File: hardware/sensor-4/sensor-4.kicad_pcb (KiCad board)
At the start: 2 copper layers, 11 x 32 mm, 13 parts, among them J101 2x05_Horizontal, U101 A31010SEHALT-10

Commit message: Replace Order_Number
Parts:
- C101: footprint Capacitor_SMD:C_0603_1608Metric -> V2_Capacitor_SMD:C_0603
- FID101, FID102: value Fiducial -> Fiducial_Paste
- H101, H102, H103: value MountingHole_2.5mm -> 2.5mm
- INFO101: value ORDER-NUMBER -> ~; footprint V2_Production:Order_Number -> V2_Production:Revision
- moved INFO101 2.30 mm to (163.8, 169.8)
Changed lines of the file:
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@@
 	(paper "A4")
 	(title_block
-		(date "2023-07-17")
-		(rev "1")
+		(date "2026-02-13")
+		(rev "2026-02-13")
 	)
 	(layers
@@
 			)
 		)
-		(property "Value" "Fiducial"
+		(property "Value" "Fiducial_Paste"
 			(at 0 1.5 0)
 			(layer "F.Fab")
@@
 			)
 		)
-		(property "Description" "Fiducial Marker"
+		(property "Description" ""
 			(at 0 0 0)
 			(unlocked yes)
@@
 		(at 159.75 171 180)
 		(property "Reference" "J101"
-			(at -1.27 -7.62 0)
+			(at -1.27 -7.62 180)
 			(layer "F.SilkS")
 			(hide yes)
@@
 					(thickness 0.065024)
 				)
-				(justify right top)
+				(justify left bottom)
 			)
 		)
 		(property "Value" "2x05_Horizontal"
-			(at -1.778 3.81 0)
+			(at -1.778 3.81 180)
 			(layer "F.Fab")
 			(hide yes)
@@
 					(thickness 0.065024)
 				)
-				(justify right top)
-			)
-		)
-		(property "Datasheet" "~"
+				(justify left bottom)
+			)
+		)
+		(property "Datasheet" ""
 			(at 0 0 180)
 			(unlocked yes)
@@
 			(end -3.175 -1.2)
 			(stroke
-				(width 0.127)
-				(type solid)
-			)
-			(layer "F.SilkS")
-		)
-		(fp_line
-			(start 3.175 -3.7)
-			(end 3.175 -1.2)
-			(stroke
-				(width 0.127)
+				(width 0.1)
 				(type solid)
 			)
@@
 			(end 3.175 -3.7)
 			(stroke
-				(width 0.127)
+				(width 0.1)
 				(type solid)
 			)
@@
 			(end 2.54 -3.7)
 			(stroke
-				(width 0.127)
+				(width 0.1)
 				(type solid)
 			)
@@
 			(end -1.27 -3.7)
 			(stroke
-				(width 0.127)
-				(type solid)
-			)
-			(layer "F.SilkS")
-		)
-		(fp_line
-			(start -3.175 -1.2)
-			(end -3.175 -3.7)
-			(stroke
-				(width 0.127)
+				(width 0.1)
 				(type solid)
 			)
@@
 			(end -2.54 -3.7)
 			(stroke
-				(width 0.127)
-				(type solid)
-			)
+				(width 0.1)
+				(type solid)
+			)
+			(layer "F.SilkS")
+		)
+		(fp_poly
+			(pts
+				(xy 4.01 0.155) (xy 3.77 -0.175) (xy 4.25 -0.175) (xy 4.01 0.155)
+			)
+			(stroke
+				(width 0.12)
+				(type solid)
+			)
+			(fill yes)
 			(layer "F.SilkS")
 		)
@@
 			)
 			(layer "F.Fab")
+		)
+		(fp_text user "${REFERENCE}"
+			(at 0 -2.4 180)
+			(layer "F.Fab")
+			(effects
+				(font
+					(size 0.5 0.5)
+					(thickness 0.1)
+					(bold yes)
+				)
+			)
 		)
 		(pad "" smd roundrect
@@
 		)
 		(embedded_fonts no)
-		(model "../../3dmodels/V2_Connector_PinHeader_1.27mm.3dshapes/PinHeader_2x05_P1.27mm.stp"
+		(model "../../3dmodels/V2_Connector_PinHeader_1.27mm.3dshapes/PinHeader_2x05_P1.27mm_Horizontal.step"
 			(offset
 				(xyz 2.52 1.18 1.65)
@@
 			)
 		)
-		(property "Value" "MountingHole_2.5mm"
+		(property "Value" "2.5mm"
 			(at 0 2.23 0)
 			(unlocked yes)
@@
 			)
 		)
-		(property "Description" "Mounting Hole without connection"
+		(property "Description" ""
 			(at 0 0 0)
 			(unlocked yes)
@@
 			)
 		)
-		(property "Value" "Fiducial"
+		(property "Value" "Fiducial_Paste"
 			(at 0 1.5 0)
 			(layer "F.Fab")
@@
 			)
 		)
-		(property "Description" "Fiducial Marker"
+		(property "Description" ""
 			(at 0 0 0)
 			(unlocked yes)
@@
 			)
 		)
-		(property "Value" "MountingHole_2.5mm"
+		(property "Value" "2.5mm"
 			(at 0 2.23 0)
 			(unlocked yes)
@@
 			)
 		)
-		(property "Description" "Mounting Hole without connection"
+		(property "Description" ""
 			(at 0 0 0)
 			(unlocked yes)
@@
 		(embedded_fonts no)
 	)
-	(footprint "Capacitor_SMD:C_0603_1608Metric"
+	(footprint "V2_Capacitor_SMD:C_0603"
 		(layer "F.Cu")
 		(at 159.75 162.75)
@@
 			)
 		)
-		(property "Datasheet" "~"
+		(property "Datasheet" ""
 			(at 0 0 0)
 			(layer "F.Fab")
@@
 			)
 		)
-		(property "Description" "Unpolarized capacitor, small symbol"
+		(property "Description" ""
 			(at 0 0 0)
 			(layer "F.Fab")
@@
 		)
 		(fp_rect
-			(start -1.48 -0.73)
-			(end 1.48 0.73)
+			(start -1.23 -0.73)
+			(end 1.23 0.73)
 			(stroke
 				(width 0.05)
@@
 			(effects
 				(font
-					(size 0.4 0.4)
-					(thickness 0.06)
-				)
-			)
+					(size 0.3 0.3)
+					(thickness 0.05)
+				)
+			)
+		)
+		(pad "" smd roundrect
+			(at -0.7 0)
+			(size 0.7 0.8)
+			(layers "F.Paste")
+			(roundrect_rratio 0.1428571429)
+			(chamfer_ratio 0.3)
+			(chamfer top_right bottom_right)
+		)
+		(pad "" smd roundrect
+			(at 0.7 0)
+			(size 0.7 0.8)
+			(layers "F.Paste")
+			(roundrect_rratio 0.1428571429)
+			(chamfer_ratio 0.3)
+			(chamfer top_left bottom_left)
 		)
 		(pad "1" smd roundrect
-			(at -0.775 0)
-			(size 0.9 0.95)
-			(layers "F.Cu" "F.Mask" "F.Paste")
-			(roundrect_rratio 0.25)
+			(at -0.7 0)
+			(size 0.7 0.8)
+			(layers "F.Cu" "F.Mask")
+			(roundrect_rratio 0.1428571429)
 			(net 1 "+3V3")
 			(pintype "passive")
 		)
 		(pad "2" smd roundrect
-			(at 0.775 0)
-			(size 0.9 0.95)
-			(layers "F.Cu" "F.Mask" "F.Paste")
-			(roundrect_rratio 0.25)
+			(at 0.7 0)
+			(size 0.7 0.8)
+			(layers "F.Cu" "F.Mask")
+			(roundrect_rratio 0.1428571429)
 			(net 4 "GND")
 			(pintype "passive")
 		)
 		(embedded_fonts no)
-		(model "${KICAD9_3DMODEL_DIR}/Capacitor_SMD.3dshapes/C_0603_1608Metric.step"
+		(model "../../3dmodels/V2_Capacitor_SMD.3dshapes/C_0603_1608Metric.step"
 			(offset
 				(xyz 0 0 0)
@@
 		)
 	)
-	(footprint "V2_Production:Order_Number"
+	(footprint "V2_Production:Revision"
 		(layer "F.Cu")
-		(at 164.25 167.5 90)
+		(at 163.75 169.75 90)
 		(property "Reference" "INFO101"
 			(at 0 -1.77 90)
@@
 			)
 		)
-		(property "Value" "ORDER-NUMBER"
+		(property "Value" "~"
 			(at 0 2.27 90)
 			(unlocked yes)
@@
 		(sheetname "/")
 		(sheetfile "sensor-4.kicad_sch")
-		(attr exclude_from_pos_files exclude_from_bom)
-		(fp_rect
-			(start -7 -0.75)
-			(end 7 0.75)
-			(stroke
-				(width 0.05)
-				(type default)
-			)
-			(fill no)
-			(layer "F.CrtYd")
-		)
-		(fp_text user "${Order-Number}"
+		(attr exclude_from_pos_files exclude_from_bom allow_missing_courtyard)
+		(fp_text user "${REVISION} (${ISSUE_DATE})"
 			(at 0 0 90)
 			(unlocked yes)
@@
 			(effects
 				(font
-					(size 0.8 0.8)
-					(thickness 0.12)
+					(size 0.75 0.75)
+					(thickness 0.1)
+				)
+			)
+		)
+		(fp_text user "${REVISION} (${ISSUE_DATE})"
+			(at 0 0 90)
+			(unlocked yes)
+			(layer "F.Fab")
+			(effects
+				(font
+					(size 0.75 0.75)
+					(thickness 0.1)
 				)
 			)
@@
 		)
 		(embedded_fonts no)
-		(model "/Users/kay/Documents/KiCad/8.0/versioduo.kicad/3dmodels/V2_Sensor_Hall.3dshapes/A31010SEHALT-10.stp"
+		(model "../../3dmodels/V2_Sensor_Hall.3dshapes/A31010SEHALT-10.stp"
 			(offset
 				(xyz 0 0 0)
@@
 			)
 		)
-		(property "Value" "MountingHole_2.5mm"
+		(property "Value" "2.5mm"
 			(at 0 2.23 0)
 			(unlocked yes)
@@
 			)
 		)
-		(property "Description" "Mounting Hole without connection"
+		(property "Description" ""
 			(at 0 0 0)
 			(unlocked yes)
@@
 		(embedded_fonts no)
 	)
-	(gr_arc
-		(start 165.25 179)
-		(mid 164.957107 179.707107)
-		(end 164.25 180)
-		(stroke
-			(width 0.05)
-			(type solid)
-		)
-		(layer "Edge.Cuts")
-	)
 	(gr_line
 		(start 154.25 149)
 		(end 154.25 177.75)
-		(stroke
-			(width 0.05)
-			(type solid)
-		)
-		(layer "Edge.Cuts")
-	)
-	(gr_line
-		(start 155.25 180)
-		(end 156.5 180)
-		(stroke
-			(width 0.05)
-			(type solid)
-		)
-		(layer "Edge.Cuts")
-	)
-	(gr_line
-		(start 163 180)
-		(end 164.25 180)
 		(stroke
 			(width 0.05)
@@
 	)
 	(gr_arc
+		(start 155.25 180)
+		(mid 154.542893 179.707107)
+		(end 154.25 179)
+		(stroke
+			(width 0.05)
+			(type solid)
+		)
+		(layer "Edge.Cuts")
+	)
+	(gr_line
+		(start 155.25 180)
+		(end 156.5 180)
+		(stroke
+			(width 0.05)
+			(type solid)
+		)
+		(layer "Edge.Cuts")
+	)
+	(gr_line
+		(start 163 180)
+		(end 164.25 180)
+		(stroke
+			(width 0.05)
+			(type solid)
+		)
+		(layer "Edge.Cuts")
+	)
+	(gr_arc
 		(start 164.25 148)
 		(mid 164.957107 148.292893)
@@
 		(layer "Edge.Cuts")
 	)
-	(gr_arc
-		(start 155.25 180)
-		(mid 154.542893 179.707107)
-		(end 154.25 179)
-		(stroke
-			(width 0.05)
-			(type solid)
-		)
-		(layer "Edge.Cuts")
-	)
 	(gr_line
 		(start 165.25 149)
@@
 		(stroke
 			(width 0.05)
+			(type solid)
+		)
+		(layer "Edge.Cuts")
+	)
+	(gr_arc
+		(start 165.25 179)
+		(mid 164.957107 179.707107)
+		(end 164.25 180)
+		(stroke
+			(width 0.05)

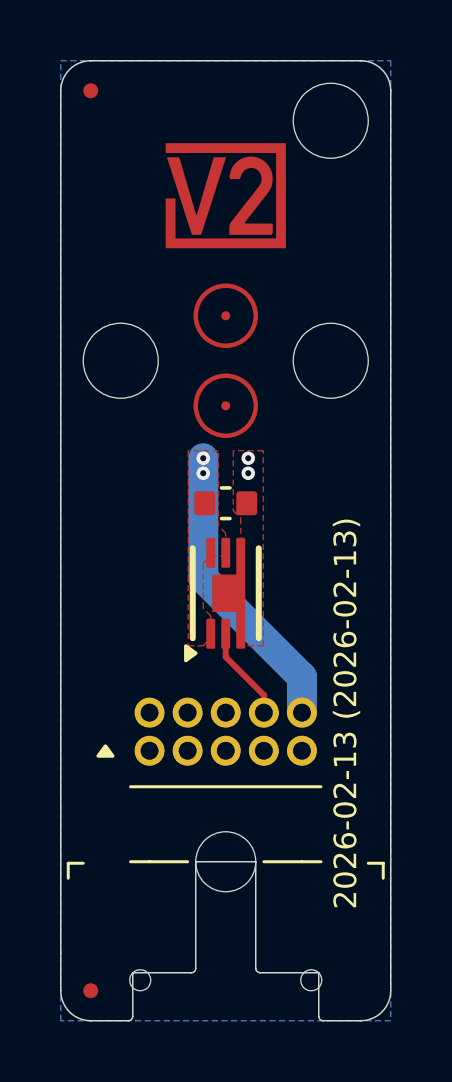
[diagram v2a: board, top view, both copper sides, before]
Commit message: KiCad 10
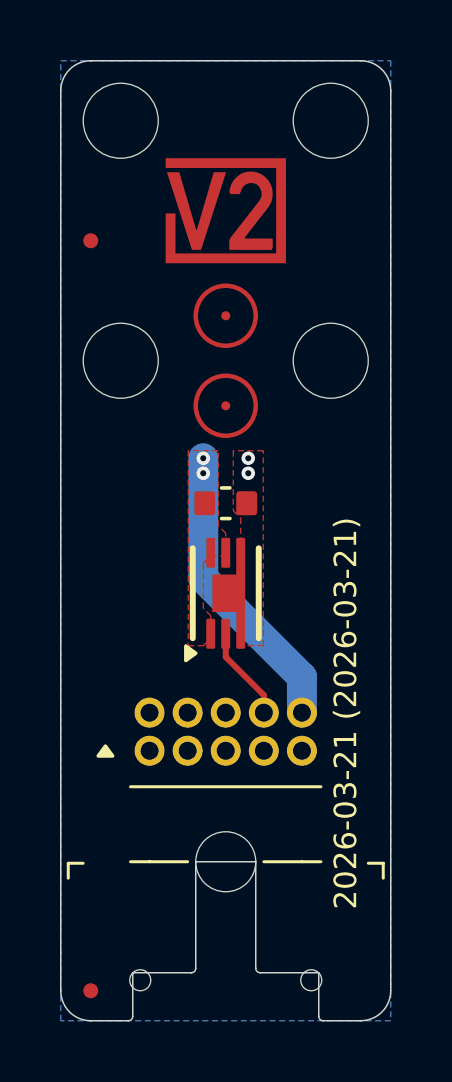
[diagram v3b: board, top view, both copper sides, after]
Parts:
- added H104: 2.5mm, V2_Mechanical:MountingHole_2.5mm, F.Cu at (156.2, 150.0)
- moved FID102 5.00 mm to (155.2, 154.0)
- moved ICON103 0.50 mm to (159.8, 153.0)
